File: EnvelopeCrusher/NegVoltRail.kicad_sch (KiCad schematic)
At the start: 8 parts

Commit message: Completed Schematic
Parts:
- added C56: 1uF, Capacitor_SMD:C_0805_2012Metric_Pad1.18x1.45mm_HandSolder, symbol Device:C
- added C57: 10uF, Capacitor_SMD:C_0805_2012Metric_Pad1.18x1.45mm_HandSolder, symbol Device:C
- added U17: SE82XX-50, Package_TO_SOT_SMD:SOT-223-3_TabPin2, symbol Regulator_Linear:AP1117-33
- C33, C34, C35, C36: renamed from C?; footprint (none) -> Capacitor_SMD:C_0805_2012Metric_Pad1.18x1.45mm_HandSolder
- gave numbers to parts that had none: 4
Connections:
- net GND: now also C56.2, C57.2, U17.1 (GND)
- new net +5V: C57.1, U17.2 (VO)
- new net +9V: C56.1, U17.3 (VI)
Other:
- moved on the sheet: C33, C34, C35, C36, D5, R18, R19, U11

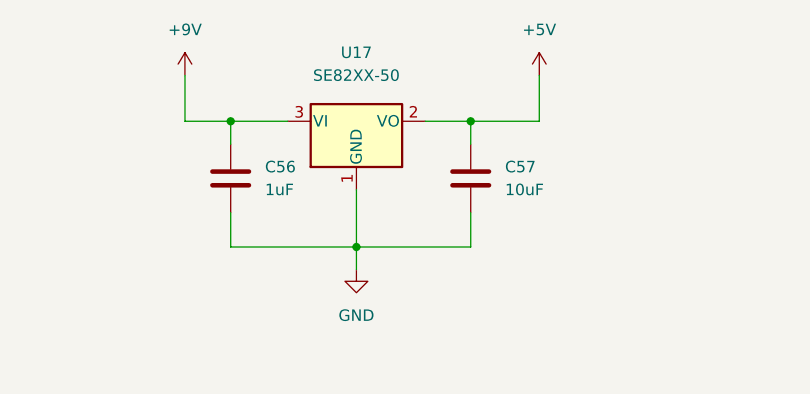
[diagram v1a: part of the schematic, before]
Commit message: Updated schematic
- Replaced CD4066 (SOIC14) with DG611 (QFN16)
- Replaced CLK/ENV mixer jumpers with 4xSPST DIPSW
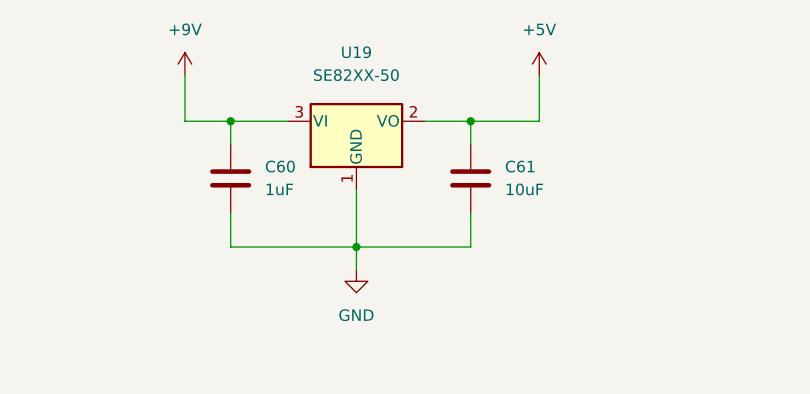
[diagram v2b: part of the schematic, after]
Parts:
- renumbered C56 to C60, C57 to C61, U17 to U19
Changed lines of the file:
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@@
   (symbol (lib_id "power:+9V") (at 125.73 46.99 0) (unit 1)
     (in_bom yes) (on_board yes) (fields_autoplaced)
-    (property "Reference" "#PWR082" (id 0) (at 125.73 50.8 0)
+    (property "Reference" "#PWR088" (id 0) (at 125.73 50.8 0)
       (effects (font (size 1.27 1.27)) hide)
     )
@@
   (symbol (lib_id "Regulator_Linear:AP1117-33") (at 144.78 52.07 0) (unit 1)
     (in_bom yes) (on_board yes) (fields_autoplaced)
-    (property "Reference" "U17" (id 0) (at 144.78 44.45 0))
+    (property "Reference" "U19" (id 0) (at 144.78 44.45 0))
     (property "Value" "SE82XX-50" (id 1) (at 144.78 46.99 0))
     (property "Footprint" "Package_TO_SOT_SMD:SOT-223-3_TabPin2" (id 2) (at 144.78 46.99 0)
@@
   (symbol (lib_id "power:+5V") (at 165.1 46.99 0) (unit 1)
     (in_bom yes) (on_board yes) (fields_autoplaced)
-    (property "Reference" "#PWR087" (id 0) (at 165.1 50.8 0)
+    (property "Reference" "#PWR090" (id 0) (at 165.1 50.8 0)
       (effects (font (size 1.27 1.27)) hide)
     )
@@
   (symbol (lib_id "power:GND") (at 144.78 68.58 0) (unit 1)
     (in_bom yes) (on_board yes) (fields_autoplaced)
-    (property "Reference" "#PWR083" (id 0) (at 144.78 74.93 0)
+    (property "Reference" "#PWR089" (id 0) (at 144.78 74.93 0)
       (effects (font (size 1.27 1.27)) hide)
     )
@@
   (symbol (lib_id "Device:C") (at 157.48 58.42 0) (unit 1)
     (in_bom yes) (on_board yes) (fields_autoplaced)
-    (property "Reference" "C57" (id 0) (at 161.29 57.1499 0)
+    (property "Reference" "C61" (id 0) (at 161.29 57.1499 0)
       (effects (font (size 1.27 1.27)) (justify left))
     )
@@
   (symbol (lib_id "Device:C") (at 130.81 58.42 0) (unit 1)
     (in_bom yes) (on_board yes) (fields_autoplaced)
-    (property "Reference" "C56" (id 0) (at 134.62 57.1499 0)
+    (property "Reference" "C60" (id 0) (at 134.62 57.1499 0)
       (effects (font (size 1.27 1.27)) (justify left))
     )

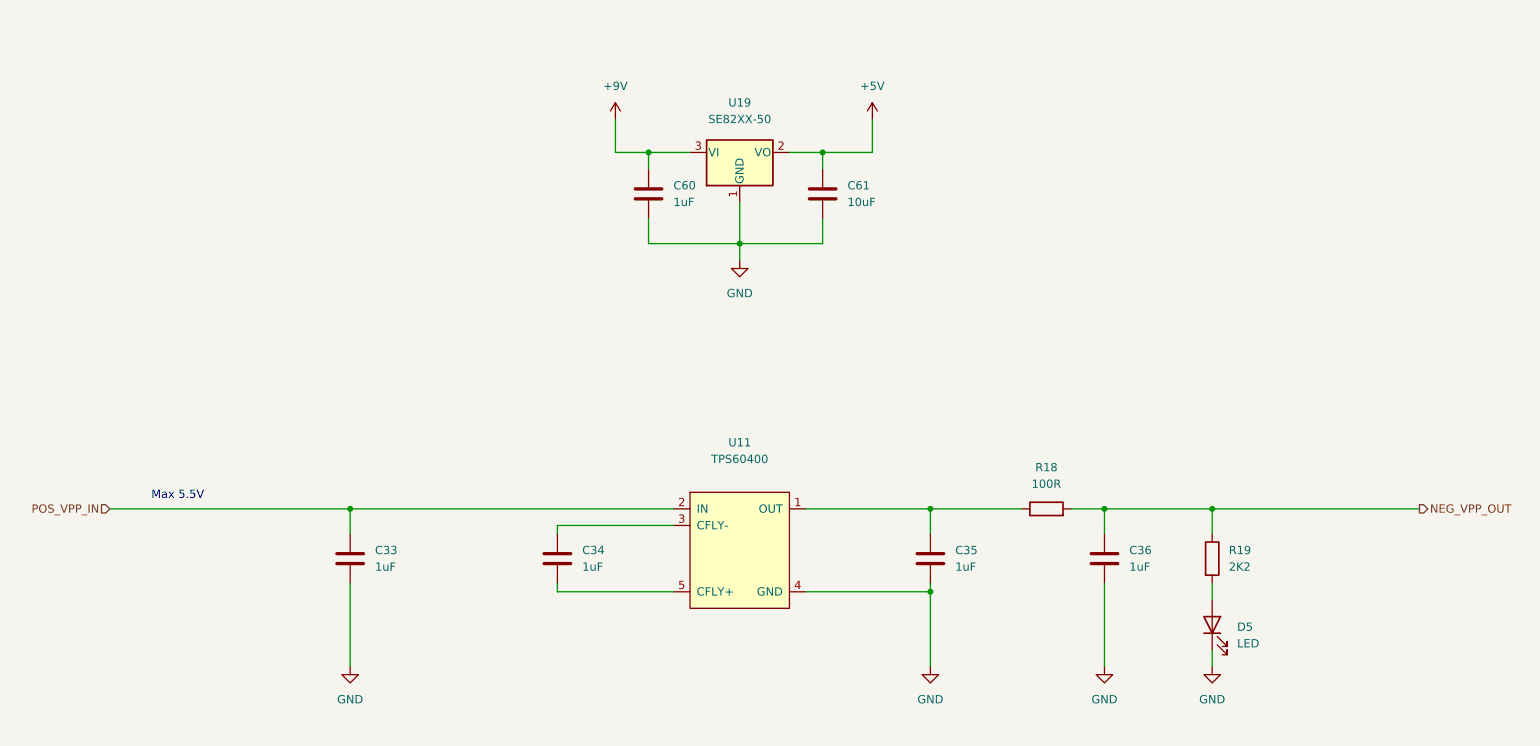
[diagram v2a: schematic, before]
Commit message: updated schematic
- Added values and comments to state-variable filter block
- Updated footprints
- Changed Dual Op Amp: TL072 to AM358
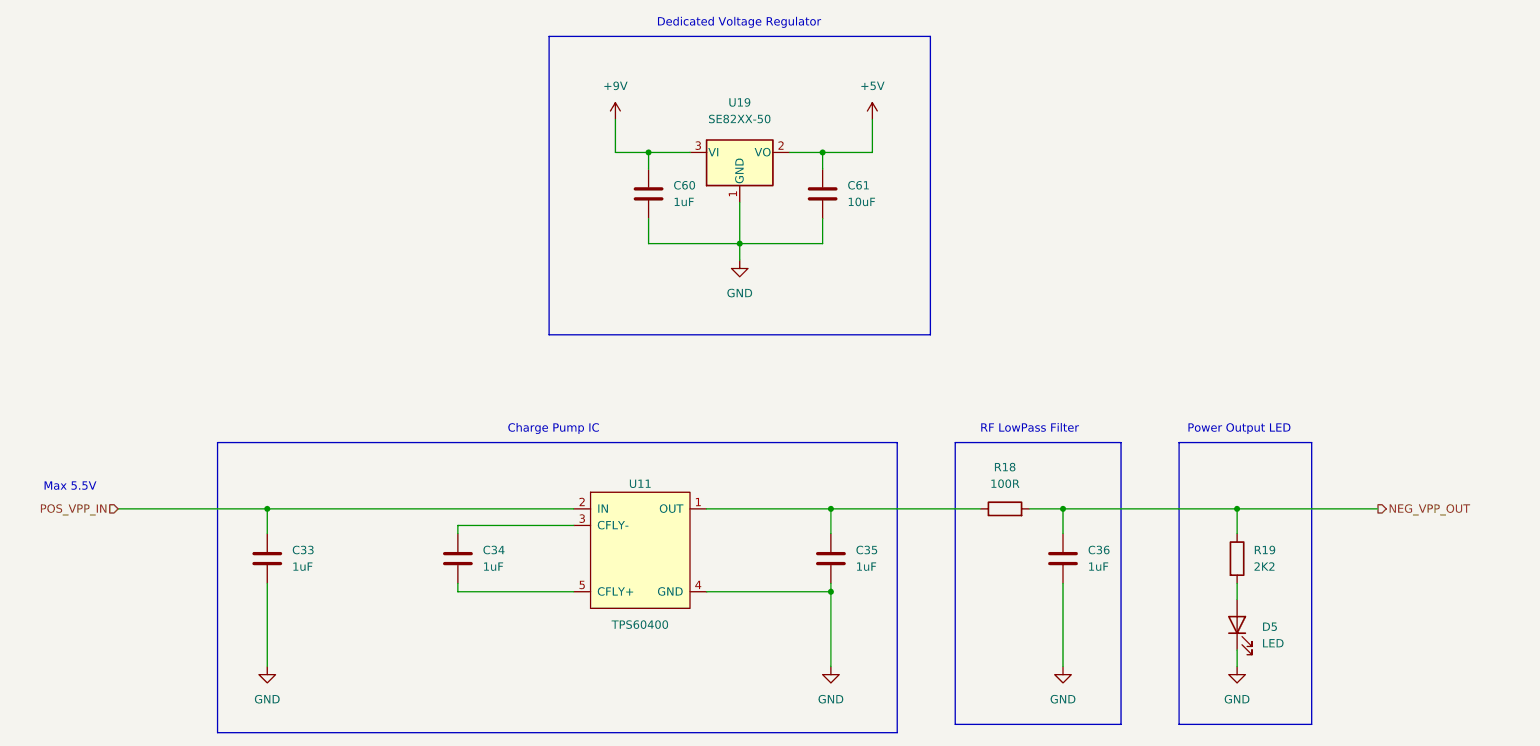
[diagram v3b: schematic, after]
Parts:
- R18, R19: footprint (none) -> Resistor_SMD:R_0805_2012Metric_Pad1.20x1.40mm_HandSolder
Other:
- note added: "Charge Pump IC"
- note added: "Dedicated Voltage Regulator"
- note added: "Power Output LED"
- note added: "RF LowPass Filter"
- moved on the sheet: C33, C34, C35, C36, D5, R18, R19, U11

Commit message: Updated footprints/symbol mappings
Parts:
- U19: footprint Package_TO_SOT_SMD:SOT-223-3_TabPin2 -> Package_TO_SOT_SMD:SOT-23
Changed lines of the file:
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@@
     (property "Reference" "U19" (id 0) (at 144.78 44.45 0))
     (property "Value" "SE82XX-50" (id 1) (at 144.78 46.99 0))
-    (property "Footprint" "Package_TO_SOT_SMD:SOT-223-3_TabPin2" (id 2) (at 144.78 46.99 0)
+    (property "Footprint" "Package_TO_SOT_SMD:SOT-23" (id 2) (at 144.78 46.99 0)
       (effects (font (size 1.27 1.27)) hide)
     )

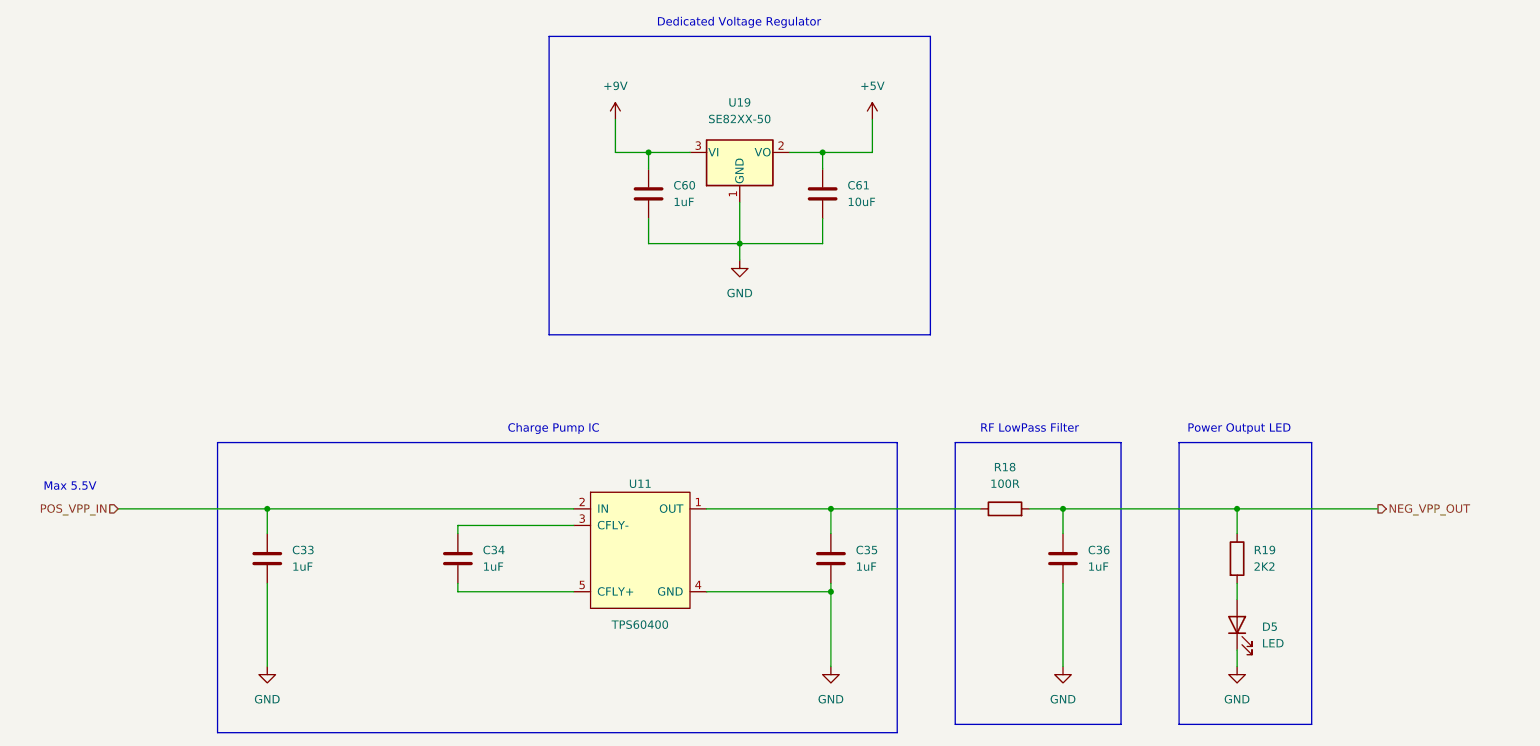
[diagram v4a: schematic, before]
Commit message: organised layout into functional blocks
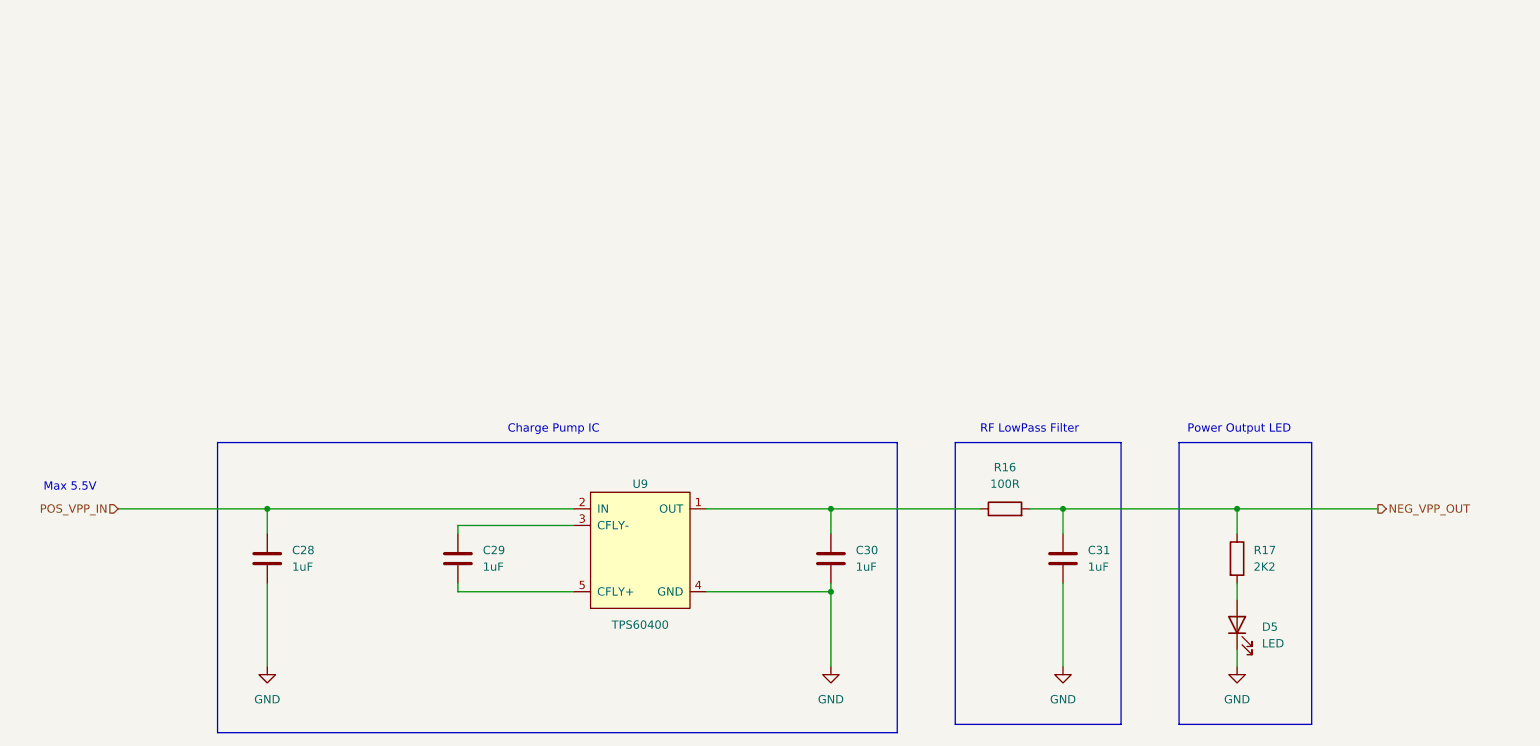
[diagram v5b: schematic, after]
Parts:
- removed C60: 1uF, Capacitor_SMD:C_0805_2012Metric_Pad1.18x1.45mm_HandSolder, symbol Device:C
- removed C61: 10uF, Capacitor_SMD:C_0805_2012Metric_Pad1.18x1.45mm_HandSolder, symbol Device:C
- removed U19: SE82XX-50, Package_TO_SOT_SMD:SOT-23, symbol Regulator_Linear:AP1117-33
- renumbered C33 to C28, C34 to C29, C35 to C30, C36 to C31, R18 to R16, R19 to R17, U11 to U9
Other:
- note removed: "Dedicated Voltage Regulator"
